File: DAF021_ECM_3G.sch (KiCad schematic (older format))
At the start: 69 parts, among them J1 Sensors, J10 USB_Argon, J11 USB_Boron, J12 USB_DEBUG, J13 Service, J14 Antenna, J20 Log, J21 Ambient Temperature, J4 Pail Sensor, J5 Horn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

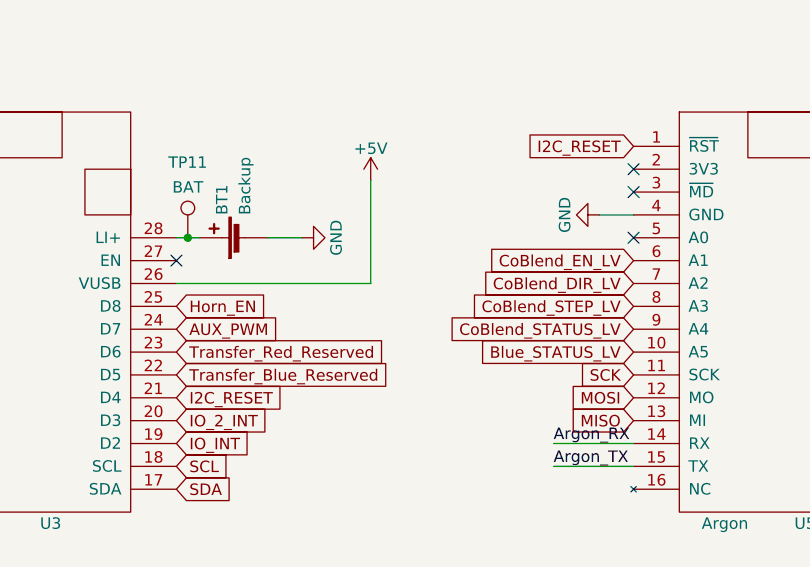
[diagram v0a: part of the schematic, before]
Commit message: MotorController interrupt bodge wire
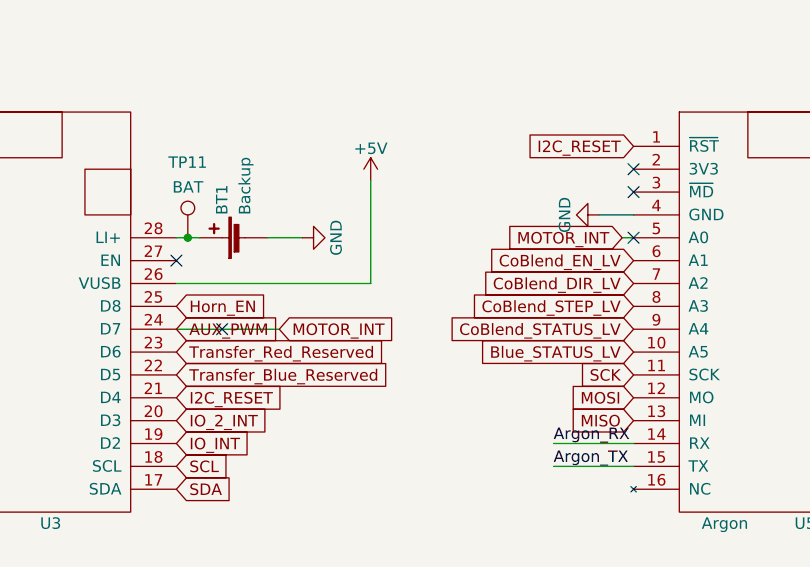
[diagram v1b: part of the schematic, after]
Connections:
- net AUX_PWM: now also U5.5 (A0)
- no-connect marks 25 -> 26
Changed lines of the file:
@@
 Text GLabel 11650 2450 0    50   Input ~ 0
 CoBlend_EN_LV
-NoConn ~ 11650 2350
 $Comp
 L MCU_Particle-VDW:Argon U5
@@
 F1 "Cable.sch" 50
 $EndSheet
+Text GLabel 11600 2350 0    50   Input ~ 0
+MOTOR_INT
+NoConn ~ 11650 2350
+Wire Wire Line
+	11600 2350 11650 2350
+Text GLabel 10100 2750 2    50   Input ~ 0
+MOTOR_INT
+Wire Wire Line
+	10100 2750 9650 2750
+NoConn ~ 9850 2750
 $EndSCHEMATC
